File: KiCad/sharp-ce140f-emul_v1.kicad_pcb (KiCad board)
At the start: 2 copper layers, 34.5 x 61.2 mm, 42 parts, among them J2 Micro_SD_Card_Det, J3 Conn_01x15, J4 Conn_01x15, J5 Conn_01x01, J6 Conn_01x01, J7 Conn_01x01, J8 Sharp PC 11-pin, J9 Conn_01x01, Q2 BSS138, Q3 BSS138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

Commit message: PCB review
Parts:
- D2, D3, D4, D5: footprint Diode_SMD:D_0805_2012Metric_Pad1.15x1.40mm_HandSolder -> Diode_SMD:D_SOD-323_HandSoldering
- moved R12 16.8 mm to (177.5, 135.6)
- moved R8 15.4 mm to (169.2, 135.6)
- moved R11 11.7 mm to (177.5, 133.3)
- moved R10 6.76 mm to (173.4, 135.6)
- moved D4 6.37 mm to (177.8, 148.9), turned to -90 degrees
- moved R13 6.11 mm to (174.2, 142.8)
- moved D5 6.05 mm to (177.9, 155.9), turned to 90 degrees
- moved R7 5.64 mm to (169.2, 133.3)
- moved R14 5.48 mm to (174.2, 140.5)
- moved R20 5.33 mm to (174.3, 147.7)
- moved Q2 5.33 mm to (170.2, 141.6)
- moved Q5 5.18 mm to (170.2, 148.8)
- moved R19 5.13 mm to (174.3, 150.0)
- moved R22 5.08 mm to (174.4, 154.8)
- moved R21 4.91 mm to (174.4, 157.1)
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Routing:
- net +3V3: track 162.1 -> 224.1 mm
- net /conn_dout: track 23.9 -> 41.5 mm
- net /conn_sel1: track 17.8 -> 35.1 mm
- net /conn_ack: track 36.1 -> 24.0 mm, vias 0 -> 1
- net /conn_sel2: track 18.6 -> 29.2 mm, vias 0 -> 1
- net CN3_6: track 13.4 -> 24.0 mm
- net CN3_1: track 30.3 -> 20.0 mm, vias 1 -> 0
- net /conn_busy: track 19.4 -> 27.0 mm
- net CN4_12: track 17.0 -> 24.2 mm
- net CN3_9: track 21.4 -> 16.1 mm, vias 1 -> 0
- net /conn_xout: track 20.0 -> 24.8 mm, vias 0 -> 1
- net CN3_13: track 13.7 -> 18.5 mm
- net /conn_din: track 27.3 -> 31.9 mm
- net CN4_11: track 22.5 -> 18.5 mm
- net /sd_cd: track 2.42 -> 5.83 mm
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
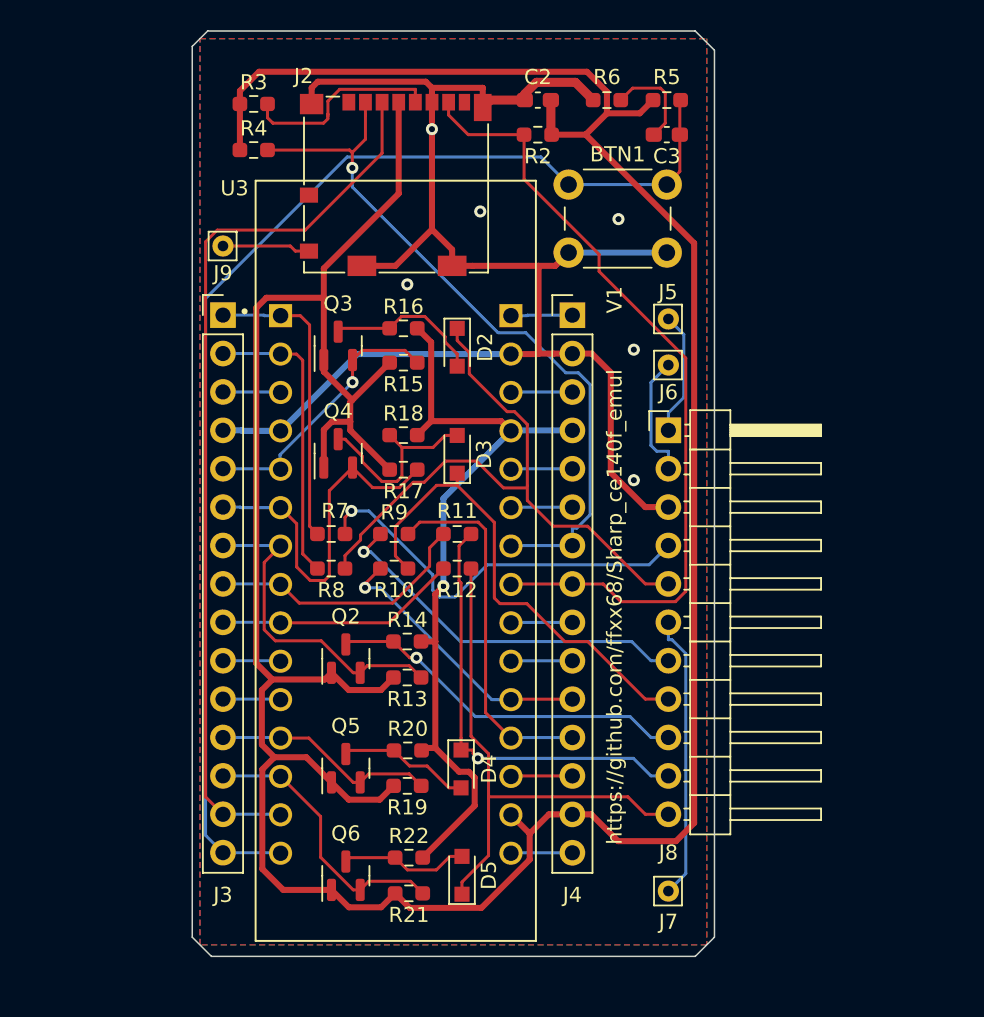
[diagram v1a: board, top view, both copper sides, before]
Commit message: some footprint review and BOM exported (csv)
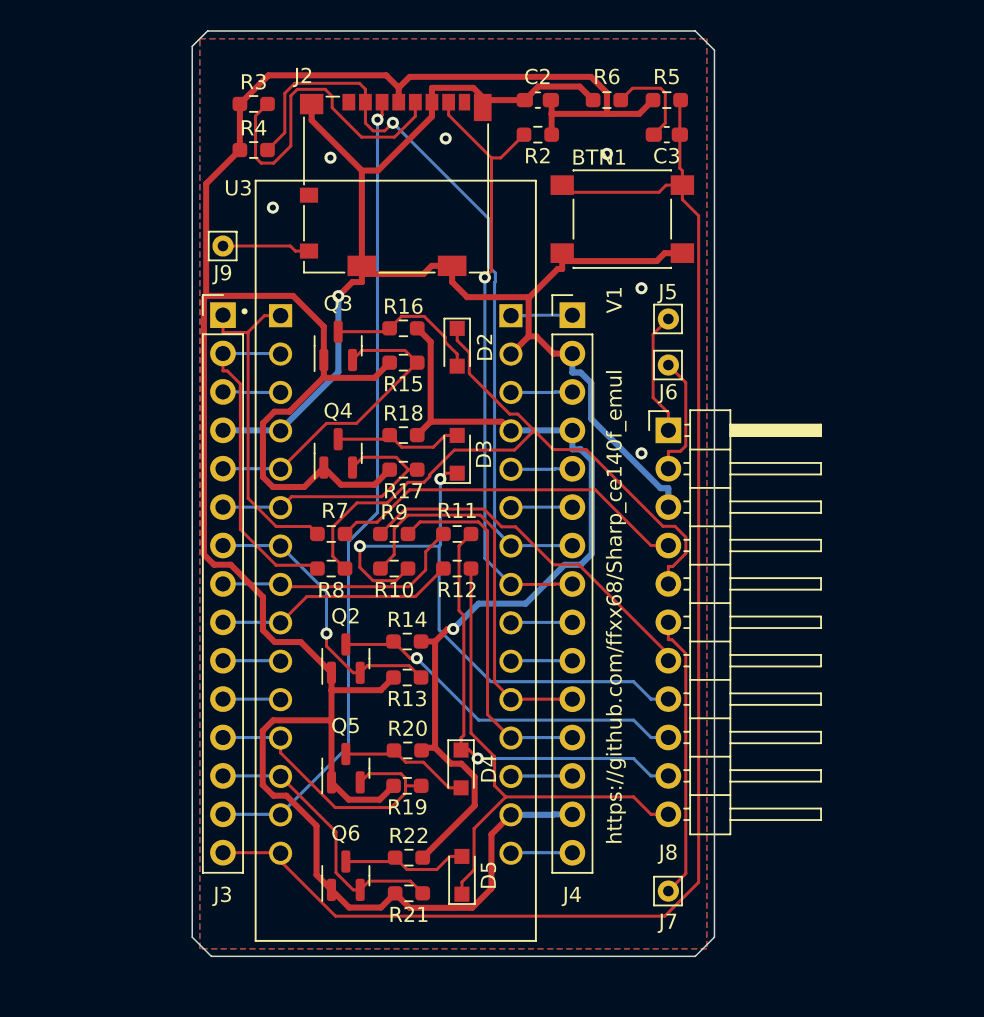
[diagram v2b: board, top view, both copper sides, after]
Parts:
- BTN1: footprint Button_Switch_THT:SW_PUSH_6mm -> Button_Switch_SMD:SW_Push_1P1T_NO_6x6mm_H9.5mm
- moved BTN1 4.23 mm to (188.5, 112.5)
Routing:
- net +3V3: track 224.1 -> 173.6 mm
- net CN3_15: track 82.1 -> 95.3 mm
- net CN4_8: track 53.4 -> 40.8 mm, vias 0 -> 1
- net /sd_sck: track 13.4 -> 21.8 mm
- net CN4_11: track 18.5 -> 26.2 mm, vias 1 -> 0
- net /conn_din: track 31.9 -> 38.9 mm, vias 0 -> 2
- net CN3_14: track 59.6 -> 53.7 mm, vias 0 -> 1
- net +5V: track 52.5 -> 58.3 mm
- net CN3_6: track 24.0 -> 18.2 mm
- net CN3_12: track 14.9 -> 20.3 mm
- net GND: track 100.8 -> 95.7 mm, vias 6 -> 7
- net /Level Conv3/conv_HV: track 12.8 -> 8.64 mm
- net /conn_dout: track 41.5 -> 45.0 mm
- net /conn_busy: track 27.0 -> 24.1 mm, vias 1 -> 0
- net CN3_5: track 17.9 -> 20.7 mm, vias 1 -> 0
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
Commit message: Final review before PCB manufacturing
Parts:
- removed BTN1: User_button, Button_Switch_SMD:SW_Push_1P1T_NO_6x6mm_H9.5mm
- removed C3: 100n, Capacitor_SMD:C_0603_1608Metric_Pad1.08x0.95mm_HandSolder
- removed D5: 1N4148, Diode_SMD:D_SOD-323_HandSoldering
- removed J9: Conn_01x01, Connector_Pin:Pin_D0.7mm_L6.5mm_W1.8mm_FlatFork
- removed Q6: BSS138, Package_TO_SOT_SMD:SOT-23
- removed U3: NUCLEO-L432KC, MyLibrary:MODULE_NUCLEO-L432KC
- added C1: 100n, Capacitor_SMD:C_0603_1608Metric_Pad1.08x0.95mm_HandSolder, F.Cu at (156.2, 147.3)
- added D1: 1N4148, Diode_SMD:D_SOD-323_HandSoldering, F.Cu at (178.0, 132.8)
- added J1: Conn_01x01, Connector_Pin:Pin_D0.7mm_L6.5mm_W1.8mm_FlatFork, F.Cu at (163.3, 148.8)
- added PB1: User_button, Button_Switch_SMD:SW_Push_1P1T_NO_6x6mm_H9.5mm, F.Cu at (162.1, 122.4)
- added Q1: BSS138, Package_TO_SOT_SMD:SOT-23, F.Cu at (191.8, 141.2)
- added R1: 47k, Resistor_SMD:R_0603_1608Metric_Pad0.98x0.95mm_HandSolder, F.Cu at (156.2, 124.0)
- added U2: NUCLEO-L432KC, MyLibrary:MODULE_NUCLEO-L432KC, F.Cu at (184.7, 137.4)
- moved R3 43.6 mm to (154.2, 147.3), turned to -90 degrees
- moved J7 40.2 mm to (207.0, 119.9), turned to 90 degrees
- moved R5 40.1 mm to (154.2, 119.6), turned to -90 degrees
- moved R21 38.8 mm to (207.5, 136.9), turned to -90 degrees
- moved R6 38.5 mm to (154.2, 124.0), turned to 90 degrees
- moved Q5 36.9 mm to (206.3, 141.2), turned to 180 degrees
- moved R22 35.4 mm to (204.9, 136.9), turned to 90 degrees
- moved R2 34.2 mm to (156.2, 128.3), turned to -90 degrees
- moved D4 32.7 mm to (206.2, 132.8), turned to 0 degrees
- moved Q4 32.1 mm to (199.0, 141.2), turned to 180 degrees
- moved J2 30.9 mm to (159.8, 137.9), turned to 90 degrees
- moved J3 30.6 mm to (168.4, 148.8), turned to 90 degrees
- moved C2 30.6 mm to (156.2, 119.6), turned to -90 degrees
- moved R19 29.0 mm to (200.2, 136.9), turned to -90 degrees
- moved R20 25.7 mm to (197.6, 136.9), turned to 90 degrees
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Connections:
- C2 pad 1: +3V3 -> CN3_15
- C2 pad 2: GND -> /rc_btn
- D2 pad 1: /conn_dout -> /conn_din
- D2 pad 2: /Level Conv2/conv_HV -> /Level Conv3/conv_HV
- D3 pad 1: /conn_din -> /conn_sel2
- D3 pad 2: /Level Conv3/conv_HV -> /Level Conv4/conv_HV
- D4 pad 1: /conn_sel2 -> /conn_sel1
- D4 pad 2: /Level Conv4/conv_HV -> /Level Conv5/conv_HV
- J2 pad 2: CN4_7 -> CN3_14
- J2 pad 3: CN3_14 -> CN4_6
- J2 pad 5: /sd_sck -> CN4_8
- J2 pad 7: CN4_8 -> CN4_7
- Q2 pad 2: CN3_7 -> CN3_5
- Q2 pad 3: /conn_ack -> /Level Conv2/conv_HV
- Q3 pad 2: CN3_5 -> CN3_6
- Q3 pad 3: /Level Conv2/conv_HV -> /Level Conv3/conv_HV
- Q4 pad 2: CN3_6 -> CN3_12
- Q4 pad 3: /Level Conv3/conv_HV -> /Level Conv4/conv_HV
- Q5 pad 2: CN3_12 -> CN3_13
- Q5 pad 3: /Level Conv4/conv_HV -> /Level Conv5/conv_HV
- R3 pad 2: /sd_sck -> CN4_6
- R4 pad 2: CN4_7 -> CN3_14
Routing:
- net CN4_6: track 4.08 -> 47.1 mm, vias 0 -> 1
- net +3V3: track 173.6 -> 135.2 mm, vias 0 -> 2
- net CN3_14: track 53.7 -> 77.4 mm, vias 1 -> 0
- net /sd_sck: track 21.8 -> 0.00 mm
- net /conn_din: track 38.9 -> 53.2 mm, vias 2 -> 1
- net /conn_dout: track 45.0 -> 32.9 mm
- net GND: track 95.7 -> 107.5 mm
- net CN4_11: track 26.2 -> 15.5 mm, vias 0 -> 1
- net CN3_13: track 18.5 -> 26.1 mm
- net CN3_5: track 20.7 -> 13.6 mm, vias 0 -> 1
- net CN3_7: track 19.2 -> 26.1 mm, vias 1 -> 0
- net CN3_12: track 20.3 -> 14.9 mm, vias 0 -> 1
- net /conn_sel1: track 34.9 -> 39.6 mm
- net CN3_6: track 18.2 -> 22.0 mm, vias 0 -> 1
- net CN4_7: track 49.8 -> 53.6 mm, vias 1 -> 2
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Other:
- board size 34.5 x 61.2 mm -> 61 x 34.5 mm
